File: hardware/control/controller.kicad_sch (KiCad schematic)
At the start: 18 parts, among them SW1 KMS221GLFS, SW2 KMS221GLFS, SW4 KMS221GLFS, U1 ESP32-C6, Y1 40MHz

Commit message: done routing
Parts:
- removed C5, C6, C7: 100n, Capacitor_SMD:C_0603_1608Metric, symbol Device:C
- added U3: W25Q128JVP, Package_SON:WSON-8-1EP_6x5mm_P1.27mm_EP3.4x4.3mm, symbol Memory_Flash:W25Q128JVP
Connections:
- net GND: now also U3.4 (GND), U3.9 (EP)
- net at U1.20 (SPICS0/GPIO24): now also U3.1 (~{CS})
- net at U1.21 (SPIQ/GPIO25): now also U3.2 (DO/IO_{1})
- net at U1.22 (SPIWP/GPIO26): now also U3.3 (~{WP}/IO_{2})
- net at U1.23 (VDD_SPI/GPIO27): now also U3.8 (VCC)
- net at U1.24 (SPIHD/GPIO28): now also U3.7 (~{HOLD}/~{RESET}/IO_{3})
- net at U1.25 (SPICLK/GPIO29): now also U3.6 (CLK)
- net at U1.26 (SPID/GPIO30): now also U3.5 (DI/IO_{0})
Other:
- moved on the sheet: C20, SW1

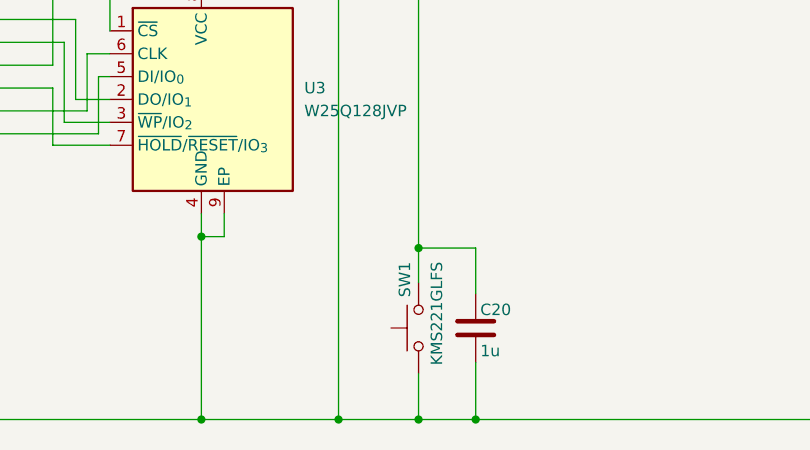
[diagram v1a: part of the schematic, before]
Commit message: changed switches due to shortage
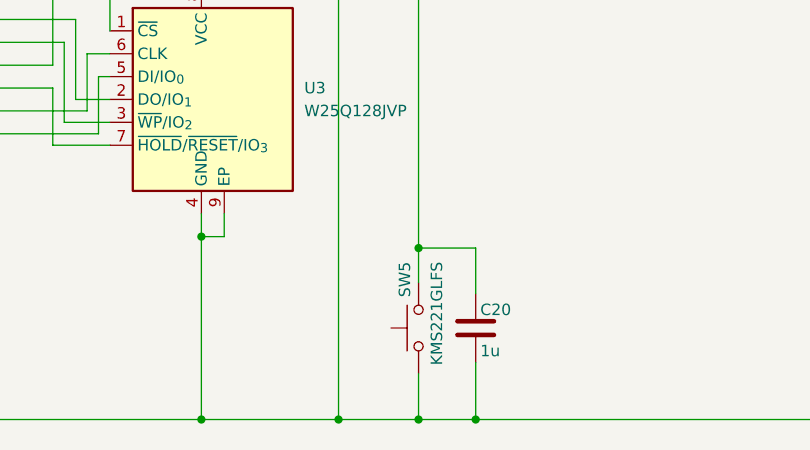
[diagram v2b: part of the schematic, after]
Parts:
- removed SW1: KMS221GLFS, Button_Switch_SMD:SW_SPST_CK_KMS2xxGP, symbol Switch:SW_Push
- added SW5: KMS221GLFS, Button_Switch_SMD:SW_SPST_TS-1088-xR020, symbol Switch:SW_Push
- SW2: footprint Button_Switch_SMD:SW_SPST_CK_KMS2xxGP -> Button_Switch_SMD:SW_SPST_TS-1088-xR020
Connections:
- net GND: now also SW5.1
- net reset: now also SW5.2
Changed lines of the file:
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@@
 			)
 		)
-		(property "Footprint" "Button_Switch_SMD:SW_SPST_CK_KMS2xxGP"
+		(property "Footprint" "Button_Switch_SMD:SW_SPST_TS-1088-xR020"
 			(at 102.87 139.7 0)
 			(hide yes)
@@
 			)
 		)
-		(property "Datasheet" "https://jlc-prod-smt.oss-eu-central-1.aliyuncs.com/smtDataManualFile/8588903737833873408-C221698.pdf?response-content-disposition=attachment%3B%20filename%3DC221698.pdf%3B%20filename%2A%3DUTF-8%27%27C221698.pdf&x-oss-date=20260604T163458Z&x-oss-expires=1800&x-oss-security-token=CAISgAN1q6Ft5B2yfSjIr5rgEov%2B1Z5Y5IPeVHLE03MEOcpBm6iagzz2IHhMdHJsAOodtv0%2FmmhT6PkclqRLcbhpcmfjV%2BZHzLB8qaJ7%2B39A4J7b16cNrbH4M4H6aXeirtuwDsz9SNTCALjPD3nPii50x5bjaDymRCbLGJaViJlhHLN1Ow6jdmhpCctxLAlvo9NgFxm3D%2Fu2NQPwiWf9FVdhvhEG6Vly8qOi2MaRmFy8yFTx0b0SvJ%2BjYMrmPctoN9JnSdC5mfdzau3a1TJ84gRD0a5wkaVA1zbDs5bfISEIuUzebreLqY03dV4mOvdqIcMe8qigz88fk%2FfIioH6xyxKOexoSCnFTOiiupCcQLPyao9jLu6iayqViY7QaIOTqQohZmkAMwVOasAsI3Ngh4zF97Qt0cVNkXO9gWfLI8DtuMleWsrkxPosAnSgc5lCkRRYwGs1287ugXlSQzo890KPDAEovaKCnZ2ZSfh7Y4sNknI6i%2Bfc2Se2MIkIBfjYxKKWD5sagAGJZBLg4dXI2cxwZhpjHr9vfG2bcnPeD2ZekO6CLDE470zoyla87k22%2FMfMgD7nSJvKHKZxx7wRTJR2C%2FIed5gUddUWOOyzyialMQCX42pgq2cGFbW2xRzddJF8rKP5p2z7HTq0AIZLZQQExEqwnA3Me1xxudMxwbz09i63yKlbRSAA&x-oss-signature-version=OSS4-HMAC-SHA256&x-oss-credential=STS.NYUY1J8AySA5VTu7sQ5Emtm1a%2F20260604%2Feu-central-1%2Foss%2Faliyun_v4_request&x-oss-signature=0287d07f1d74dc173e35fdd16bbbdb40a7eb09e1df544025205ab3d6ea2886b8"
+		(property "Datasheet" "https://jlc-prod-smt.oss-eu-central-1.aliyuncs.com/smtDataManualFile/8588886944055513088-C720477.pdf?response-content-disposition=attachment%3B%20filename%3DC720477.pdf%3B%20filename%2A%3DUTF-8%27%27C720477.pdf&x-oss-date=20260613T095523Z&x-oss-expires=1800&x-oss-security-token=CAISgAN1q6Ft5B2yfSjIr5nbM%2F7DpZ4X8vGyW3bIlkM%2BZ9lDpIDymDz2IHhMdHJsAOodtv0%2FmmhT6PkclqRLcbhpcmfjV%2BZHzLB8qbU3tGRF4J7b16cNrbH4M4H6aXeirtuwDsz9SNTCALjPD3nPii50x5bjaDymRCbLGJaViJlhHLN1Ow6jdmhpCctxLAlvo9NgFxm3D%2Fu2NQPwiWf9FVdhvhEG6Vly8qOi2MaRmFy8yFTx0b0SvJ%2BjYMrmPctoN9JnSdC5mfdzau3a1TJ84gRD0a5wkaVA1zbDs5bfISEIuUzebreLqY03dV4mOvdqIcMe8qigz88fk%2FfIioH6xyxKOexoSCnFTOiiupCcQLPyao9jLu6iayqViY7QaIOTqQohZmkAMwVOasAsI3Ngh4zF97Qt0cVNkXO9gWfLI8DtuMleWkpqA555GAPyAFpORa%2Bb5wchMHn6pr9EWOXuJZUIn3b%2FstWNupKq5ldctHSeoXq108CXVnU5PXYIKTIPXqKWD5sagAEUO2GYpMOHNmUI2aeoltsuhn2q5tYPfVojnLMFuBgbyRMlLEVrSl%2BAiNbyqebA0zMto18kd9JWF41J9ol8FzjNd6v2n4DpME8rNHRehrn63Wkk3UuD5A7%2Bzf0pEXK1OmFeKTwmPUZJh0%2FkQvdbVSeP7V92bvUvinYc69H1ZcazxCAA&x-oss-signature-version=OSS4-HMAC-SHA256&x-oss-credential=STS.NZnxDwHA6E3YYPyrCkkVoKEYz%2F20260613%2Feu-central-1%2Foss%2Faliyun_v4_request&x-oss-signature=0882924d2430544bba2cc0b02233edb855cf6e0e71f1bc6decfb309c8d97d8e2"
 			(at 102.87 139.7 0)
 			(hide yes)
@@
 			)
 		)
-		(property "Description" "C221698"
+		(property "Description" "C720477"
 			(at 107.95 139.7 0)
 			(hide yes)
@@
 	)
 	(symbol
-		(lib_id "Switch:SW_Push")
-		(at 228.6 139.7 90)
-		(unit 1)
-		(body_style 1)
-		(exclude_from_sim no)
-		(in_bom yes)
-		(on_board yes)
-		(in_pos_files yes)
-		(dnp no)
-		(property "Reference" "SW1"
-			(at 227.076 132.334 0)
-			(show_name no)
-			(do_not_autoplace no)
-			(effects
-				(font
-					(size 1.27 1.27)
-				)
-				(justify right)
-			)
-		)
-		(property "Value" "KMS221GLFS"
-			(at 230.632 132.334 0)
-			(show_name no)
-			(do_not_autoplace no)
-			(effects
-				(font
-					(size 1.27 1.27)
-				)
-				(justify right)
-			)
-		)
-		(property "Footprint" "Button_Switch_SMD:SW_SPST_CK_KMS2xxGP"
-			(at 223.52 139.7 0)
-			(hide yes)
-			(show_name no)
-			(do_not_autoplace no)
-			(effects
-				(font
-					(size 1.27 1.27)
-				)
-			)
-		)
-		(property "Datasheet" "https://jlc-prod-smt.oss-eu-central-1.aliyuncs.com/smtDataManualFile/8588903737833873408-C221698.pdf?response-content-disposition=attachment%3B%20filename%3DC221698.pdf%3B%20filename%2A%3DUTF-8%27%27C221698.pdf&x-oss-date=20260604T163458Z&x-oss-expires=1800&x-oss-security-token=CAISgAN1q6Ft5B2yfSjIr5rgEov%2B1Z5Y5IPeVHLE03MEOcpBm6iagzz2IHhMdHJsAOodtv0%2FmmhT6PkclqRLcbhpcmfjV%2BZHzLB8qaJ7%2B39A4J7b16cNrbH4M4H6aXeirtuwDsz9SNTCALjPD3nPii50x5bjaDymRCbLGJaViJlhHLN1Ow6jdmhpCctxLAlvo9NgFxm3D%2Fu2NQPwiWf9FVdhvhEG6Vly8qOi2MaRmFy8yFTx0b0SvJ%2BjYMrmPctoN9JnSdC5mfdzau3a1TJ84gRD0a5wkaVA1zbDs5bfISEIuUzebreLqY03dV4mOvdqIcMe8qigz88fk%2FfIioH6xyxKOexoSCnFTOiiupCcQLPyao9jLu6iayqViY7QaIOTqQohZmkAMwVOasAsI3Ngh4zF97Qt0cVNkXO9gWfLI8DtuMleWsrkxPosAnSgc5lCkRRYwGs1287ugXlSQzo890KPDAEovaKCnZ2ZSfh7Y4sNknI6i%2Bfc2Se2MIkIBfjYxKKWD5sagAGJZBLg4dXI2cxwZhpjHr9vfG2bcnPeD2ZekO6CLDE470zoyla87k22%2FMfMgD7nSJvKHKZxx7wRTJR2C%2FIed5gUddUWOOyzyialMQCX42pgq2cGFbW2xRzddJF8rKP5p2z7HTq0AIZLZQQExEqwnA3Me1xxudMxwbz09i63yKlbRSAA&x-oss-signature-version=OSS4-HMAC-SHA256&x-oss-credential=STS.NYUY1J8AySA5VTu7sQ5Emtm1a%2F20260604%2Feu-central-1%2Foss%2Faliyun_v4_request&x-oss-signature=0287d07f1d74dc173e35fdd16bbbdb40a7eb09e1df544025205ab3d6ea2886b8"
-			(at 223.52 139.7 0)
-			(hide yes)
-			(show_name no)
-			(do_not_autoplace no)
-			(effects
-				(font
-					(size 1.27 1.27)
-				)
-			)
-		)
-		(property "Description" "C221698"
-			(at 228.6 139.7 0)
-			(hide yes)
-			(show_name no)
-			(do_not_autoplace no)
-			(effects
-				(font
-					(size 1.27 1.27)
-				)
-			)
-		)
-		(pin "1"
-		)
-		(pin "2"
-		)
-		(instances
-			(project "control"
-				(path "/a48bfc30-bdab-4a84-8176-692a115cc595/c74e1f1d-22f4-4f9d-8f80-7a60d3f285ae"
-					(reference "SW1")
-					(unit 1)
-				)
-			)
-		)
-	)
-	(symbol
 		(lib_id "Device:R")
 		(at 69.85 49.53 0)
@@
 					(unit 1)
 				)
+			)
+		)
+	)
+	(symbol
+		(lib_id "Switch:SW_Push")
+		(at 228.6 139.7 90)
+		(unit 1)
+		(body_style 1)
+		(exclude_from_sim no)
+		(in_bom yes)
+		(on_board yes)
+		(in_pos_files yes)
+		(dnp no)
+		(property "Reference" "SW5"
+			(at 227.076 132.334 0)
+			(show_name no)
+			(do_not_autoplace no)
+			(effects
+				(font
+					(size 1.27 1.27)
+				)
+				(justify right)
+			)
+		)
+		(property "Value" "KMS221GLFS"
+			(at 230.632 132.334 0)
+			(show_name no)
+			(do_not_autoplace no)
+			(effects
+				(font
+					(size 1.27 1.27)
+				)
+				(justify right)
+			)
+		)
+		(property "Footprint" "Button_Switch_SMD:SW_SPST_TS-1088-xR020"
+			(at 223.52 139.7 0)
+			(hide yes)
+			(show_name no)
+			(do_not_autoplace no)
+			(effects
+				(font
+					(size 1.27 1.27)
+				)
+			)
+		)
+		(property "Datasheet" "https://jlc-prod-smt.oss-eu-central-1.aliyuncs.com/smtDataManualFile/8588886944055513088-C720477.pdf?response-content-disposition=attachment%3B%20filename%3DC720477.pdf%3B%20filename%2A%3DUTF-8%27%27C720477.pdf&x-oss-date=20260613T095523Z&x-oss-expires=1800&x-oss-security-token=CAISgAN1q6Ft5B2yfSjIr5nbM%2F7DpZ4X8vGyW3bIlkM%2BZ9lDpIDymDz2IHhMdHJsAOodtv0%2FmmhT6PkclqRLcbhpcmfjV%2BZHzLB8qbU3tGRF4J7b16cNrbH4M4H6aXeirtuwDsz9SNTCALjPD3nPii50x5bjaDymRCbLGJaViJlhHLN1Ow6jdmhpCctxLAlvo9NgFxm3D%2Fu2NQPwiWf9FVdhvhEG6Vly8qOi2MaRmFy8yFTx0b0SvJ%2BjYMrmPctoN9JnSdC5mfdzau3a1TJ84gRD0a5wkaVA1zbDs5bfISEIuUzebreLqY03dV4mOvdqIcMe8qigz88fk%2FfIioH6xyxKOexoSCnFTOiiupCcQLPyao9jLu6iayqViY7QaIOTqQohZmkAMwVOasAsI3Ngh4zF97Qt0cVNkXO9gWfLI8DtuMleWkpqA555GAPyAFpORa%2Bb5wchMHn6pr9EWOXuJZUIn3b%2FstWNupKq5ldctHSeoXq108CXVnU5PXYIKTIPXqKWD5sagAEUO2GYpMOHNmUI2aeoltsuhn2q5tYPfVojnLMFuBgbyRMlLEVrSl%2BAiNbyqebA0zMto18kd9JWF41J9ol8FzjNd6v2n4DpME8rNHRehrn63Wkk3UuD5A7%2Bzf0pEXK1OmFeKTwmPUZJh0%2FkQvdbVSeP7V92bvUvinYc69H1ZcazxCAA&x-oss-signature-version=OSS4-HMAC-SHA256&x-oss-credential=STS.NZnxDwHA6E3YYPyrCkkVoKEYz%2F20260613%2Feu-central-1%2Foss%2Faliyun_v4_request&x-oss-signature=0882924d2430544bba2cc0b02233edb855cf6e0e71f1bc6decfb309c8d97d8e2"
+			(at 223.52 139.7 0)
+			(hide yes)
+			(show_name no)
+			(do_not_autoplace no)
+			(effects
+				(font
+					(size 1.27 1.27)
+				)
+			)
+		)
+		(property "Description" "C720477"
+			(at 228.6 139.7 0)
+			(hide yes)
+			(show_name no)
+			(do_not_autoplace no)
+			(effects
+				(font
+					(size 1.27 1.27)
+				)
+			)
+		)
+		(pin "1"
+		)
+		(pin "2"
+		)
+		(instances
+			(project "control"
+				(path "/a48bfc30-bdab-4a84-8176-692a115cc595/c74e1f1d-22f4-4f9d-8f80-7a60d3f285ae"
+					(reference "SW5")
+					(unit 1)
+				)
